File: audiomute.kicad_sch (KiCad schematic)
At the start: 21 parts, among them J1 MJ-3523-SMT, J4 MJ-3523-SMT, Q1 MMBT3904, Q2 MMBT3906, Q3 MMBT3904, Q4 MMBT3904

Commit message: Minor updates to layout and created new gerbers and drills.
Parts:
- J2, J3: value (none) -> B2B-XH-A_LF__SN_; footprint (none) -> digikey-footprints:PinHeader_1x2_P2.5mm_Drill1.1mm
- Q1, Q3, Q4: value MMBT3904 -> NPN
- Q2: value MMBT3906 -> PNP
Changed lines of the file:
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@@
       (effects (font (size 1.27 1.27)) (justify left))
     )
-    (property "Value" "MMBT3906" (id 1) (at 149.6314 103.3022 0)
+    (property "Value" "PNP" (id 1) (at 149.6314 103.3022 0)
       (effects (font (size 1.27 1.27)) (justify left))
     )
@@
       (effects (font (size 1.27 1.27)) (justify left))
     )
-    (property "Value" "MMBT3904" (id 1) (at 131.8514 118.5422 0)
+    (property "Value" "NPN" (id 1) (at 131.8514 118.5422 0)
       (effects (font (size 1.27 1.27)) (justify left))
     )
@@
       (effects (font (size 1.27 1.27)) (justify left))
     )
-    (property "Value" "MMBT3904" (id 1) (at 162.3314 119.8122 0)
+    (property "Value" "NPN" (id 1) (at 162.3314 119.8122 0)
       (effects (font (size 1.27 1.27)) (justify left))
     )
@@
     (in_bom yes) (on_board yes) (fields_autoplaced)
     (property "Reference" "J2" (id 0) (at 97.79 111.9972 90))
-    (property "Value" "" (id 1) (at 97.79 114.5341 90))
-    (property "Footprint" "" (id 2) (at 104.14 121.92 0)
+    (property "Value" "B2B-XH-A_LF__SN_" (id 1) (at 97.79 114.5341 90))
+    (property "Footprint" "digikey-footprints:PinHeader_1x2_P2.5mm_Drill1.1mm" (id 2) (at 104.14 121.92 0)
       (effects (font (size 1.524 1.524)) (justify left) hide)
     )
@@
       (effects (font (size 1.27 1.27)) (justify left))
     )
-    (property "Value" "MMBT3904" (id 1) (at 187.7314 119.8122 0)
+    (property "Value" "NPN" (id 1) (at 187.7314 119.8122 0)
       (effects (font (size 1.27 1.27)) (justify left))
     )
@@
     (in_bom yes) (on_board yes) (fields_autoplaced)
     (property "Reference" "J3" (id 0) (at 100.33 95.4872 90))
-    (property "Value" "" (id 1) (at 100.33 98.0241 90))
-    (property "Footprint" "" (id 2) (at 106.68 105.41 0)
+    (property "Value" "B2B-XH-A_LF__SN_" (id 1) (at 100.33 98.0241 90))
+    (property "Footprint" "digikey-footprints:PinHeader_1x2_P2.5mm_Drill1.1mm" (id 2) (at 106.68 105.41 0)
       (effects (font (size 1.524 1.524)) (justify left) hide)
     )
@@
     )
     (path "/185e829f-2552-4105-840f-92799e71a280"
-      (reference "Q1") (unit 1) (value "MMBT3904") (footprint "Package_TO_SOT_SMD:SOT-23")
+      (reference "Q1") (unit 1) (value "NPN") (footprint "Package_TO_SOT_SMD:SOT-23")
     )
     (path "/16c8b92f-96de-43c6-befb-6bfee5b95fc6"
-      (reference "Q2") (unit 1) (value "MMBT3906") (footprint "Package_TO_SOT_SMD:SOT-23")
+      (reference "Q2") (unit 1) (value "PNP") (footprint "Package_TO_SOT_SMD:SOT-23")
     )
     (path "/45ab6588-080b-44bd-a20f-3c136dd830f1"
-      (reference "Q3") (unit 1) (value "MMBT3904") (footprint "Package_TO_SOT_SMD:SOT-23")
+      (reference "Q3") (unit 1) (value "NPN") (footprint "Package_TO_SOT_SMD:SOT-23")
     )
     (path "/ada9f860-520a-4111-ae60-ed8770ea640f"
-      (reference "Q4") (unit 1) (value "MMBT3904") (footprint "Package_TO_SOT_SMD:SOT-23")
+      (reference "Q4") (unit 1) (value "NPN") (footprint "Package_TO_SOT_SMD:SOT-23")
     )
     (path "/d9ab214c-1521-4805-b231-e96924b752cc"

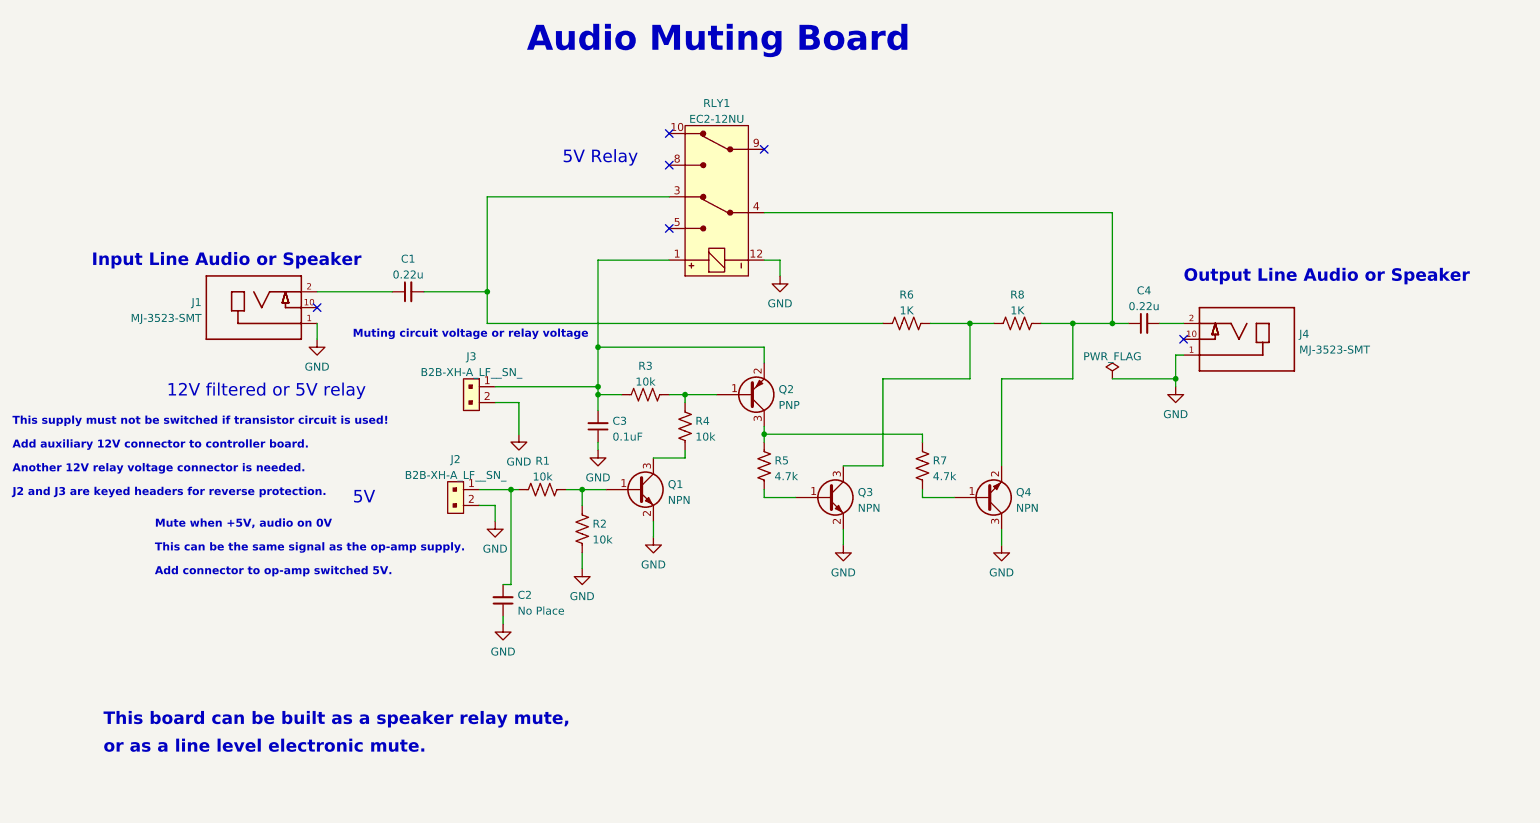
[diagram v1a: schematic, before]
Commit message: Updated schematic with stereo connectors to allow differential speaker.
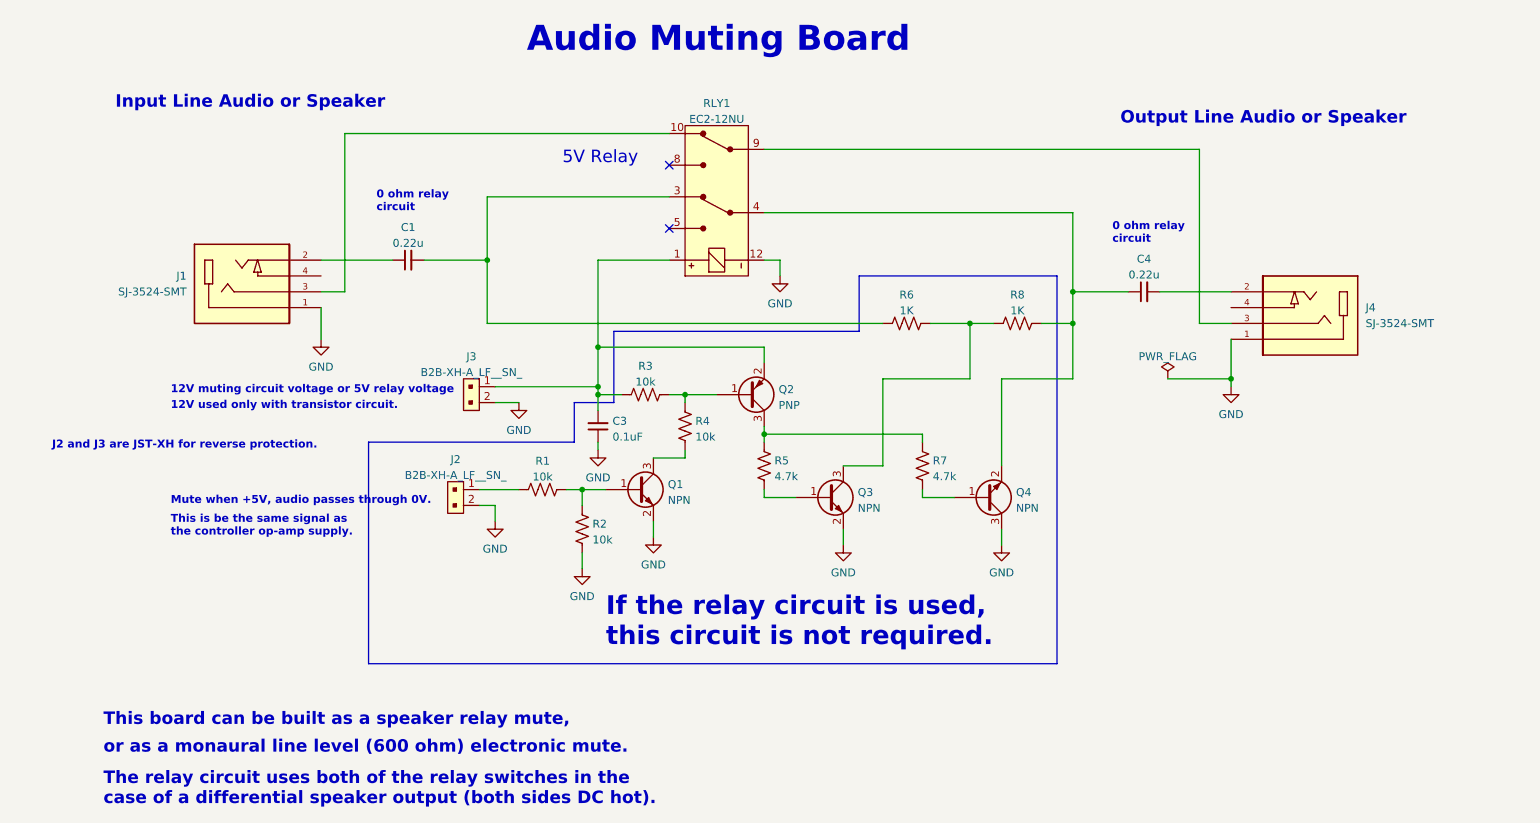
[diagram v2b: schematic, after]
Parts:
- removed C2: No Place, Capacitor_SMD:C_1206_3216Metric_Pad1.33x1.80mm_HandSolder, symbol Device:C_Small
- removed J1, J4: MJ-3523-SMT, MJ-3523-SMT:CUI_MJ-3523-SMT, symbol MJ-3523-SMT:MJ-3523-SMT
- added J1, J4: SJ-3524-SMT, CUI_SJ-3524-SMT, symbol SJ-3524-SMT:SJ-3524-SMT
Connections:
- net GND: now also J1.1, J4.1
- net at C1.1: now also J1.2
- net at C4.2: now also J4.2
- net at RLY1.10 (NC2): now also J1.3
- net at RLY1.9 (COM2): now also J4.3
- no-connect marks 6 -> 2
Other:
- note added: "0 ohm relay circuit"
- note added: "12V muting circuit voltage or 5V relay voltage"
- note added: "12V used only with transistor circuit."
- note added: "If the relay circuit is used, this circuit is not required."
- note added: "J2 and J3 are JST-XH for reverse protection."
- note added: "Mute when +5V, audio passes through 0V."
- note added: "The relay circuit uses both of the relay switches in the case of a differential speaker output (both sides DC hot)."
- note added: "This is be the same signal as the controller op-amp supply."
- note added: "or as a monaural line level (600 ohm) electronic mute."
- note removed: "12V filtered or 5V relay"
- note removed: "5V"
- note removed: "Add auxiliary 12V connector to controller board."
- note removed: "Add connector to op-amp switched 5V."
- note removed: "Another 12V relay voltage connector is needed."
- note removed: "J2 and J3 are keyed headers for reverse protection."
- note removed: "Mute when +5V, audio on 0V"
- note removed: "Muting circuit voltage or relay voltage"
- note removed: "This can be the same signal as the op-amp supply."
- note removed: "This supply must not be switched if transistor circuit is used!"
- note removed: "or as a line level electronic mute."
- moved on the sheet: C1, C4
